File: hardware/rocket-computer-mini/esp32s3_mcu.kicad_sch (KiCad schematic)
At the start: 40 parts, among them J5 Conn_01x04, SW3 R-667995, U11 GD5F2GQ5UEYIGR, U13 W25Q128JVSIQ, U14 479480001, U15 ESP32-S3RH2, U29 TPS22810DRVR, Y1 ABS07-32.768KHZ-T, Y2 ECS-400-10-37B2-CKY-TR

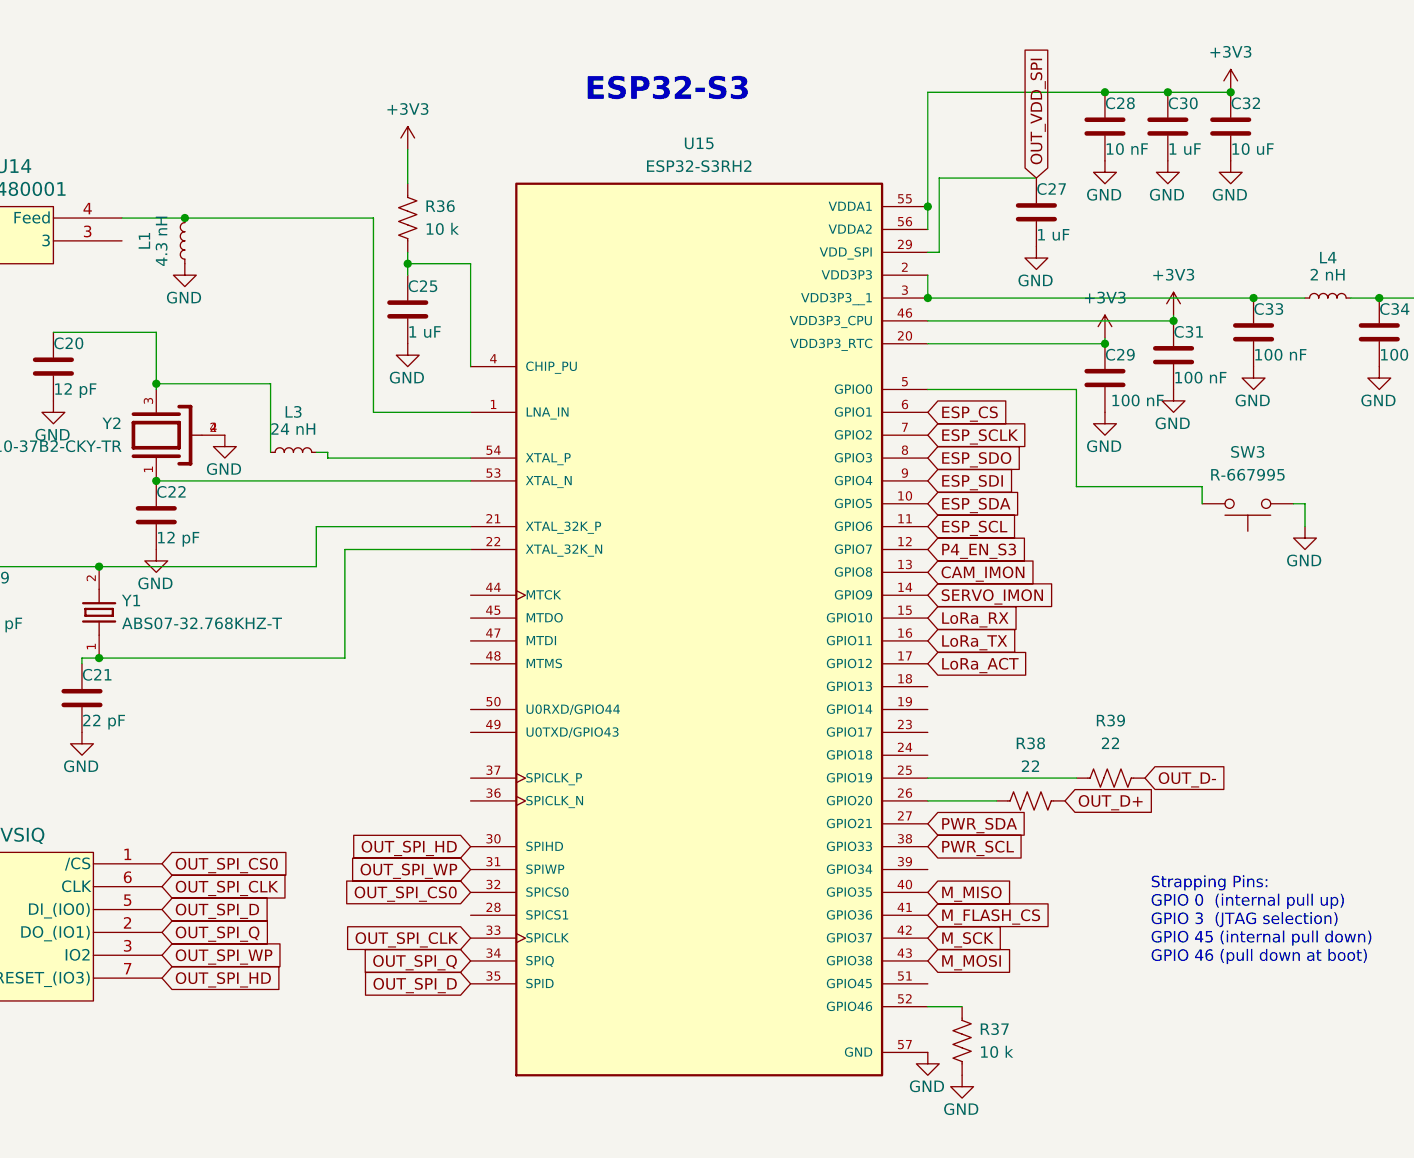
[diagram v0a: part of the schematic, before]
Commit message: hardware: rocket-computer-mini drops the ESP32-P4, S3 becomes MCU
First reduction pass. The ESP32-P4 is removed entirely and the ESP32-S3 is now
the only processor on the board, so it is no longer called OUT.

Removed -- the whole Central Processing - ESP32-P4 sheet, 65 parts: U17 (the
P4), U16 its SPI flash, U20 its dedicated TLV62569 buck, Y3/Y4 its crystals,
SW2, LEDs D7/D8 and 57 passives. Parts 255 -> 190, nets 234 -> 191, sheets
5 -> 4. Schematic and PCB both land on 190; no reference to the P4 sheet
remains in either.

Renamed -- sheet OUT - ESP32-S3 Outputs becomes MCU - ESP32-S3 in
esp32s3_mcu.kicad_sch, and the nine OUT_* nets become MCU_*. Pin names that
merely contain OUT (VOUT, OUT_17, Net-(U28-OUT)) were matched on the full
quoted net name so they were left untouched. The power-sheet note claiming
"ESP32-OUT ... enables Flight Computer" described the S3 gating the P4 and was
reworded; the topology behind it has not been rethought.

PCB -- the 65 footprints deleted, then 419 copper items (400 segments, 19
vias) removed from the 43 nets left with no pads at all, then zones refilled.

Known and deliberate: the P4 owned nearly every subsystem, so 34 named signals
are now down to a single endpoint -- sensors, all four pyro channels, all
twelve EXP lines, camera, piezo, servo, the ESP_* link and P4_EN_HOLD. Nothing
is rewired to the S3 yet and the board cannot fly as it stands.

DRC goes 28 -> 88 and every pre-existing category went down; the whole rise is
66 track_dangling + 2 via_dangling, stubs to former P4 pads on nets that still
have pads elsewhere. Left in place: these nets are about to be rewired and the
region re-laid-out, so trimming now is work the next pass would discard.
Unconnected is still 0, ERC 1012 -> 823, parity 11 -> 8.

Also stale, recorded not fixed: bom.csv is still V9's 255-part BOM, and the
on-board fab note still cites QFN-104 (U17) as the reason for ENIG.

Co-Authored-By: Claude Opus 5 <noreply@anthropic.com>
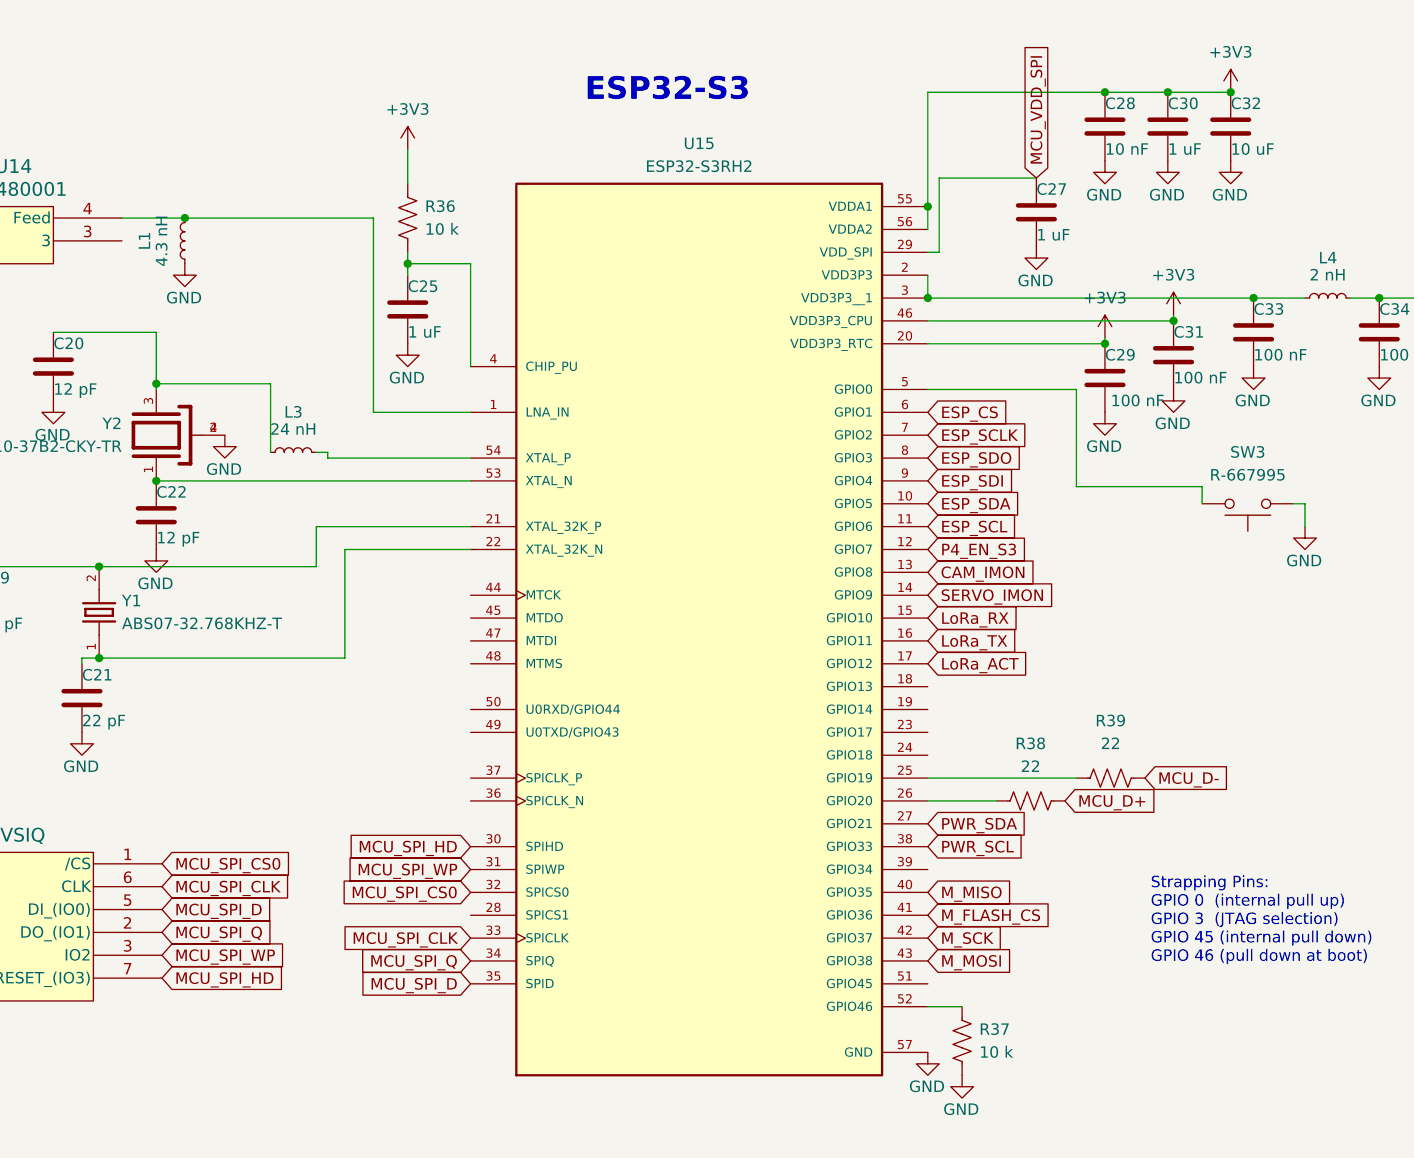
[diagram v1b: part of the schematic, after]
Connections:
- net OUT_D+ renamed MCU_D+
- net OUT_D- renamed MCU_D-
- net OUT_SPI_CLK renamed MCU_SPI_CLK
- net OUT_SPI_CS0 renamed MCU_SPI_CS0
- net OUT_SPI_D renamed MCU_SPI_D
- net OUT_SPI_HD renamed MCU_SPI_HD
- net OUT_SPI_Q renamed MCU_SPI_Q
- net OUT_SPI_WP renamed MCU_SPI_WP
- net OUT_VDD_SPI renamed MCU_VDD_SPI
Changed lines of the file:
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@@
 		)
 	)
-	(global_label "OUT_SPI_CS0"
+	(global_label "MCU_SPI_CS0"
 		(shape input)
 		(at 127.635 103.505 0)
@@
 		)
 	)
-	(global_label "OUT_SPI_WP"
+	(global_label "MCU_SPI_WP"
 		(shape input)
 		(at 161.925 104.14 180)
@@
 		)
 	)
-	(global_label "OUT_SPI_Q"
+	(global_label "MCU_SPI_Q"
 		(shape input)
 		(at 161.925 114.3 180)
@@
 		)
 	)
-	(global_label "OUT_SPI_HD"
+	(global_label "MCU_SPI_HD"
 		(shape input)
 		(at 161.925 101.6 180)
@@
 		)
 	)
-	(global_label "OUT_SPI_CLK"
+	(global_label "MCU_SPI_CLK"
 		(shape input)
 		(at 127.635 106.045 0)
@@
 		)
 	)
-	(global_label "OUT_SPI_WP"
+	(global_label "MCU_SPI_WP"
 		(shape input)
 		(at 127.635 113.665 0)
@@
 		)
 	)
-	(global_label "OUT_SPI_Q"
+	(global_label "MCU_SPI_Q"
 		(shape input)
 		(at 127.635 111.125 0)
@@
 		)
 	)
-	(global_label "OUT_SPI_D"
+	(global_label "MCU_SPI_D"
 		(shape input)
 		(at 127.635 108.585 0)
@@
 		)
 	)
-	(global_label "OUT_SPI_CS0"
+	(global_label "MCU_SPI_CS0"
 		(shape input)
 		(at 161.925 106.68 180)
@@
 		)
 	)
-	(global_label "OUT_D+"
+	(global_label "MCU_D+"
 		(shape input)
 		(at 227.965 96.52 0)
@@
 		)
 	)
-	(global_label "OUT_D-"
+	(global_label "MCU_D-"
 		(shape input)
 		(at 236.855 93.98 0)
@@
 		)
 	)
-	(global_label "OUT_SPI_D"
+	(global_label "MCU_SPI_D"
 		(shape input)
 		(at 161.925 116.84 180)
@@
 		)
 	)
-	(global_label "OUT_SPI_HD"
+	(global_label "MCU_SPI_HD"
 		(shape input)
 		(at 127.635 116.205 0)
@@
 		)
 	)
-	(global_label "OUT_VDD_SPI"
+	(global_label "MCU_VDD_SPI"
 		(shape input)
 		(at 224.79 27.305 90)
@@
 		)
 	)
-	(global_label "OUT_SPI_CLK"
+	(global_label "MCU_SPI_CLK"
 		(shape input)
 		(at 161.925 111.76 180)

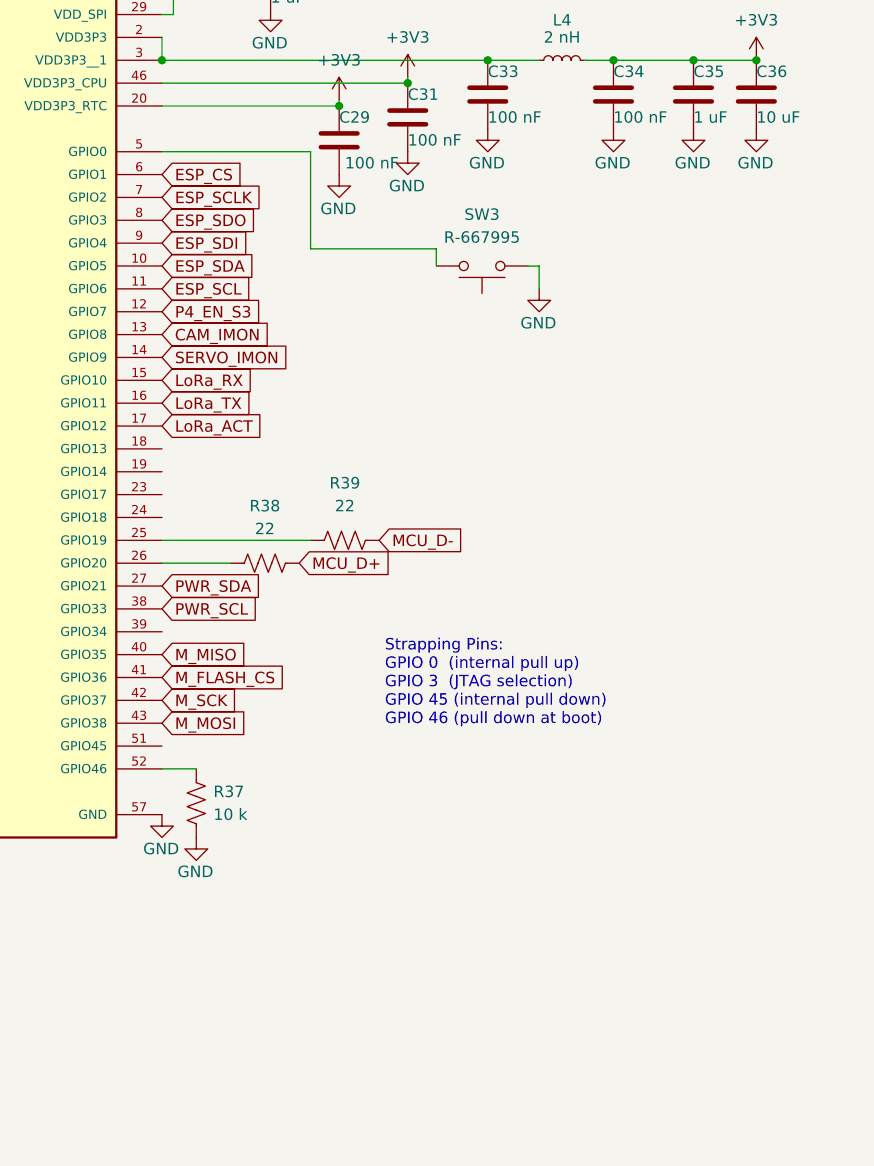
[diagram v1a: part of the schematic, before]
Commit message: hardware: rocket-computer-mini gains the on-board radio, sheds more parts
Second reduction pass, plus the radio moves on-board.

Added: the 900 MHz radio module (U16) and its two decoupling caps, wired for
direct SPI rather than through the daughterboard connector. Removed: 31
designators including the camera connector (J4), the piezo (LS1), mounting
hardware (H5-H8), and the support parts that went with them. Also gone are the
magnetometer interrupt and the inertial sensor's second interrupt -- neither was
ever used by firmware, which is what made them free to drop.

Parts 190 -> 161, nets 191 -> 165.

Adds a pin budget for the reduced board (pin-budget.md). The headline is that
the board fits, but not comfortably: 23 signals against 27 usable pads, and only
16 of those pads are free of strapping, console, JTAG or flash-adjacent duty.

Three findings shaped it:

- The radio needs seven pins, not nine. DIO2 drives transmit-enable inside the
  module and needs no processor pin; receive-enable is floating and has no
  firmware pin at all. The out-computer firmware still carries the direct-SPI
  driver from the V7 topology and defines exactly those seven, so putting the
  bare module back on-board is a board change rather than a firmware rewrite.
- Pyro continuity is a digital read, not analogue, and nothing on this board
  needs an ADC channel -- so the ADC2-versus-radio restriction does not
  constrain the design.
- Continuity belongs on an I2C expander, not a multiplexer. A four-to-one mux
  needs two select lines plus data, saving one pin; the expander shares the bus
  the magnetometer is joining and saves four.

The proposed assignment keeps the serial console free and spends JTAG. Pyro
firing is confined to unrestricted pins -- never a strapping pin and never one
the boot ROM drives, since the console transmit pin is active on every boot.

One assumption can invalidate it: three signals sit on flash-adjacent pads that
are free only if the package carries no in-pa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
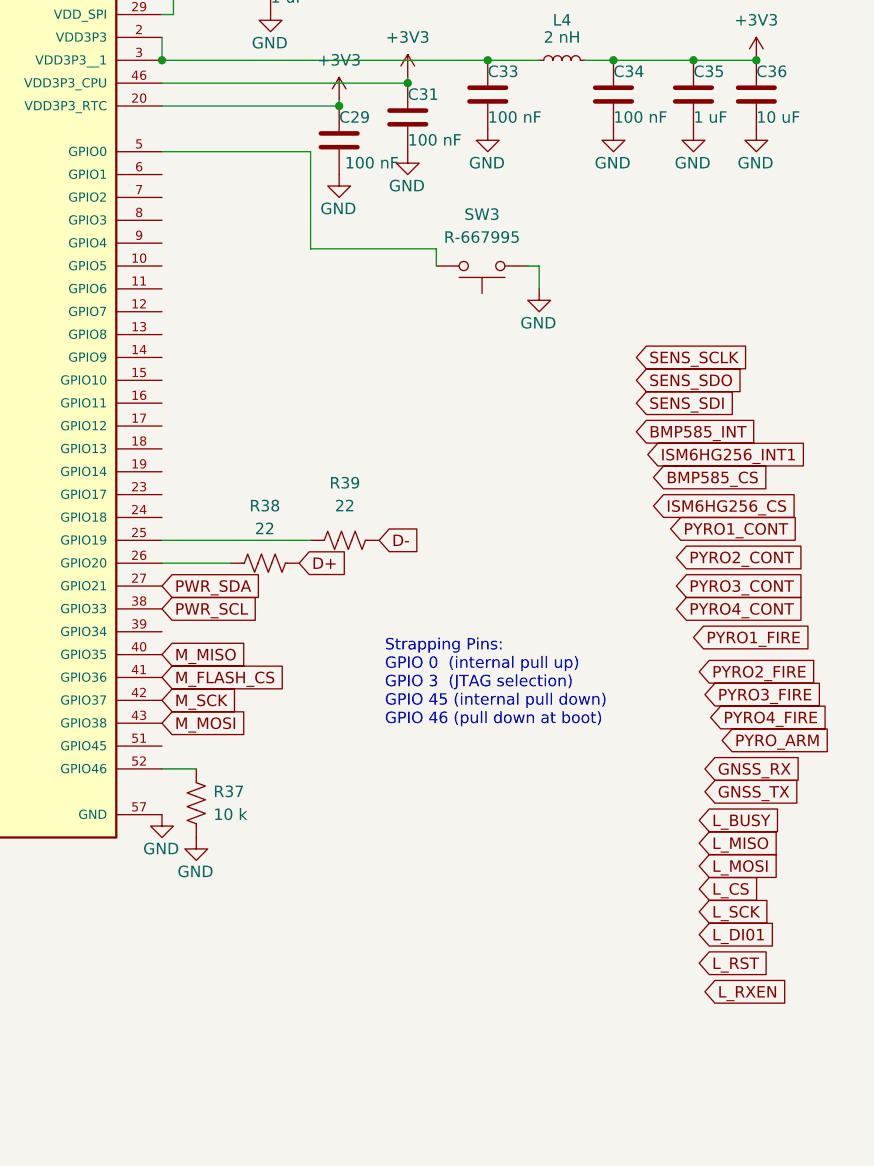
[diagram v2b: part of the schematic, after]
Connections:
- net LoRa_ACT: no longer U15.17 (GPIO12)
- net LoRa_RX: no longer U15.15 (GPIO10)
- net LoRa_TX: no longer U15.16 (GPIO11)
- net CAM_IMON: no longer names the net of U15.13 (GPIO8)
- net ESP_CS: no longer names the net of U15.6 (GPIO1)
- net ESP_SCL: no longer names the net of U15.11 (GPIO6)
- net ESP_SCLK: no longer names the net of U15.7 (GPIO2)
- net ESP_SDA: no longer names the net of U15.10 (GPIO5)
- net ESP_SDI: no longer names the net of U15.9 (GPIO4)
- net ESP_SDO: no longer names the net of U15.8 (GPIO3)
- net MCU_D+ renamed D+
- net MCU_D- renamed D-
- net P4_EN_S3: no longer names the net of U15.12 (GPIO7)
- net SERVO_IMON: no longer names the net of U15.14 (GPIO9)
